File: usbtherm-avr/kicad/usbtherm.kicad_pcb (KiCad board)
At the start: 2 copper layers, 18 parts, among them IC1 ATMEGA328-P, P1 USB_A, Q1 TMP36, Y1 12 MHz

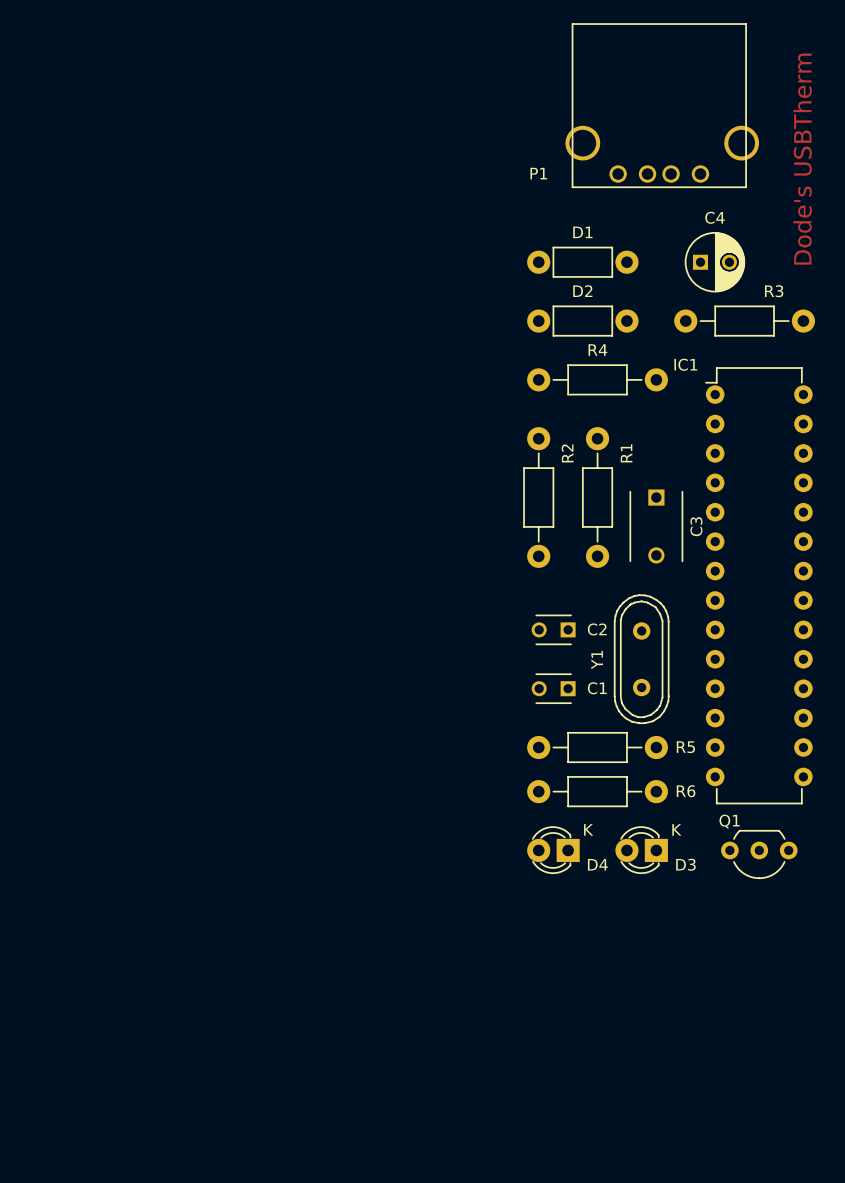
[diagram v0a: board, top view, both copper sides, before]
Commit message: replaced USB connector with plug, created footprint for it, added board edges, autorouted with FreeRouting, fixed offset of 3D model of resistors
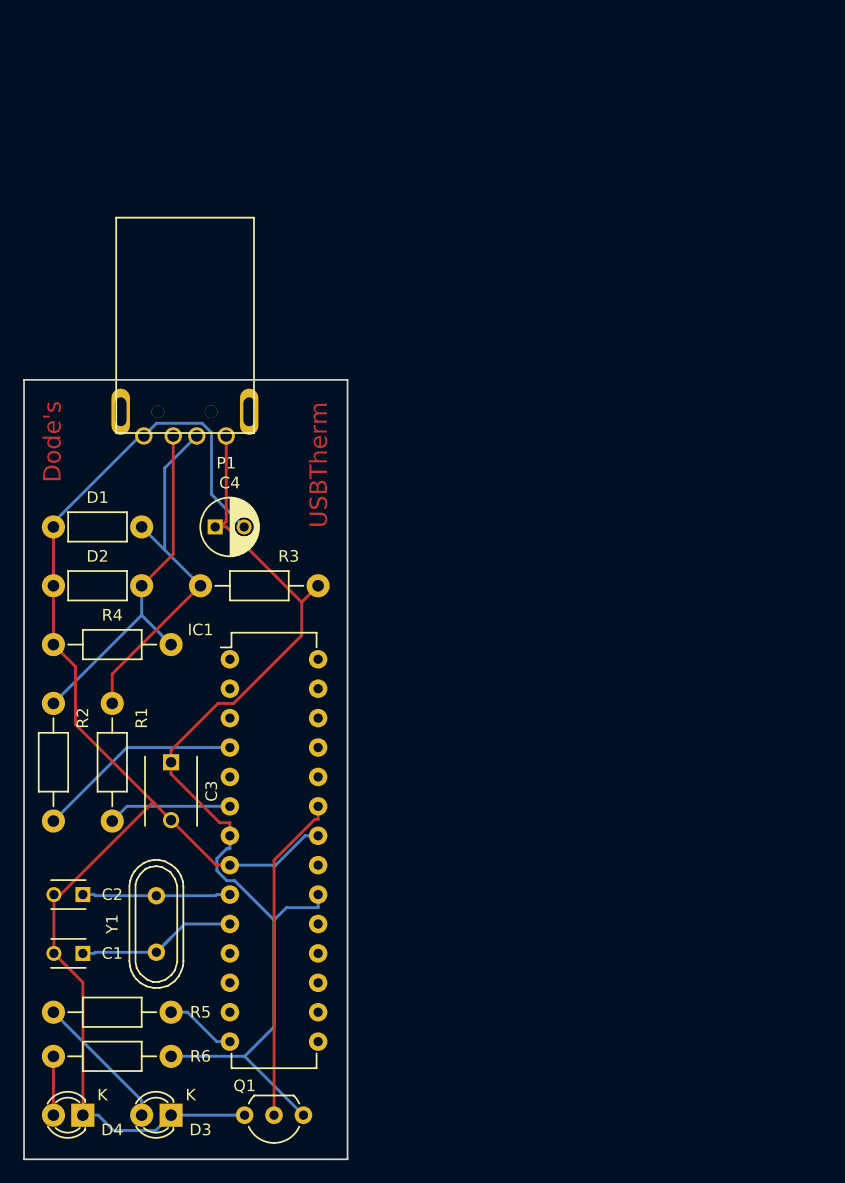
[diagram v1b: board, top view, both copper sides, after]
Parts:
- P1: value USB_A -> USB_A_PLUG; footprint Connect:USB_A -> Connect:USB_A_PLUG
- moved D1 47.7 mm to (139.7, 86.4)
- moved D2 47.7 mm to (139.7, 91.4)
- moved Q1 47.7 mm to (153.7, 137.2)
- moved C3 47.7 mm to (142.2, 106.7)
- moved R5 47.7 mm to (132.1, 128.3)
- moved R6 47.7 mm to (142.2, 132.1)
- moved C1 47.7 mm to (134.6, 123.2)
- moved C2 47.7 mm to (134.6, 118.1)
- moved C4 47.7 mm to (146.1, 86.4)
- moved D3 47.7 mm to (142.2, 137.2)
- moved D4 47.7 mm to (134.6, 137.2)
- moved IC1 47.7 mm to (147.3, 97.8)
- moved R1 47.7 mm to (137.2, 101.6)
- moved R2 47.7 mm to (132.1, 101.6)
- moved R3 47.7 mm to (154.9, 91.4)
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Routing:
- net GND: track 0.00 -> 119.5 mm
- net Net-(C3-Pad1): track 0.00 -> 90.6 mm
- net Net-(D1-Pad1): track 0.00 -> 31.5 mm
- net Net-(D2-Pad1): track 0.00 -> 31.0 mm
- net Net-(IC1-Pad23): track 0.00 -> 28.4 mm
- net Net-(IC1-Pad4): track 0.00 -> 17.9 mm
- net Net-(C1-Pad1): track 0.00 -> 15.5 mm
- net Net-(C2-Pad1): track 0.00 -> 12.8 mm
- net Net-(D3-Pad2): track 0.00 -> 12.0 mm
- net Net-(IC1-Pad6): track 0.00 -> 10.7 mm
- net Net-(IC1-Pad14): track 0.00 -> 6.13 mm
- net Net-(D4-Pad2): track 0.00 -> 5.08 mm
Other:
- board outline added: 27.9 x 67.3 mm
- board text added: "Dode's"
- board text added: "USBTherm"
- board text removed: "Dode's USBTherm"

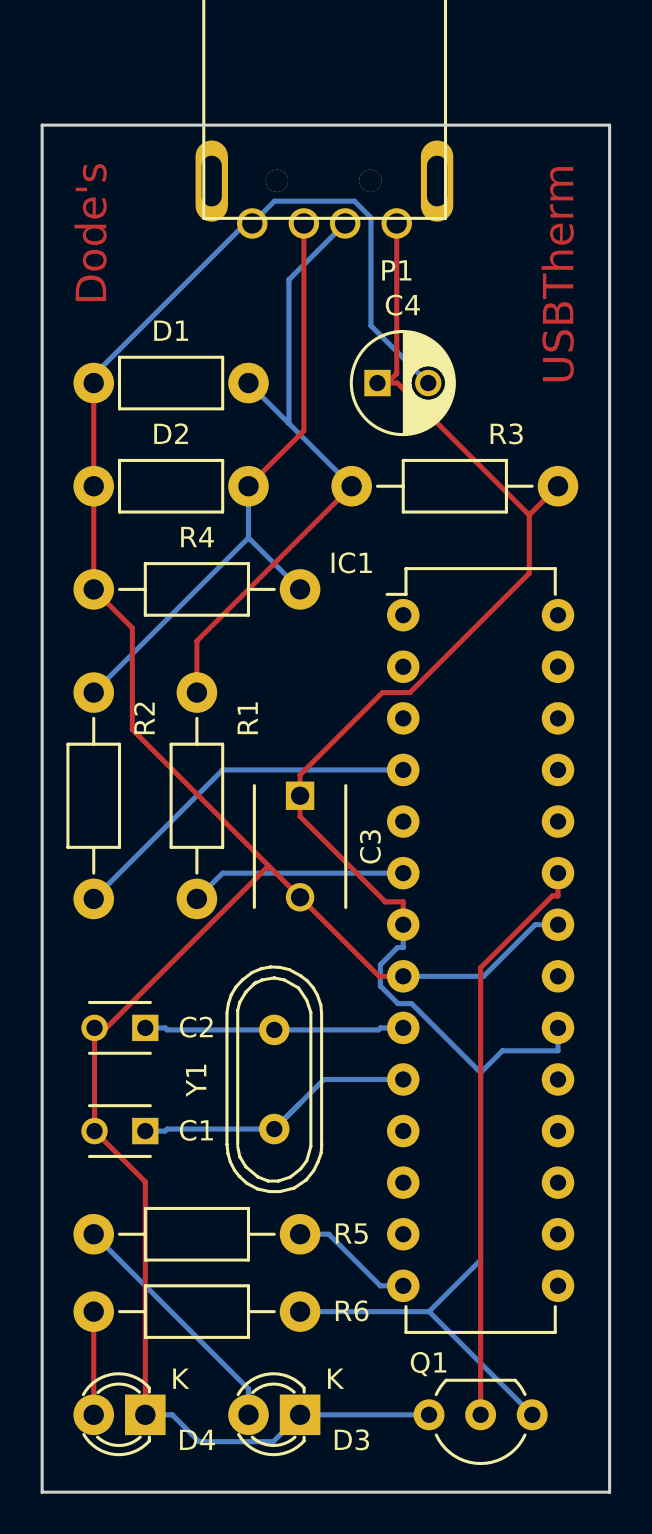
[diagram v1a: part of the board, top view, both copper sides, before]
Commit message: fixed 2 DRC warnings, added ground plane
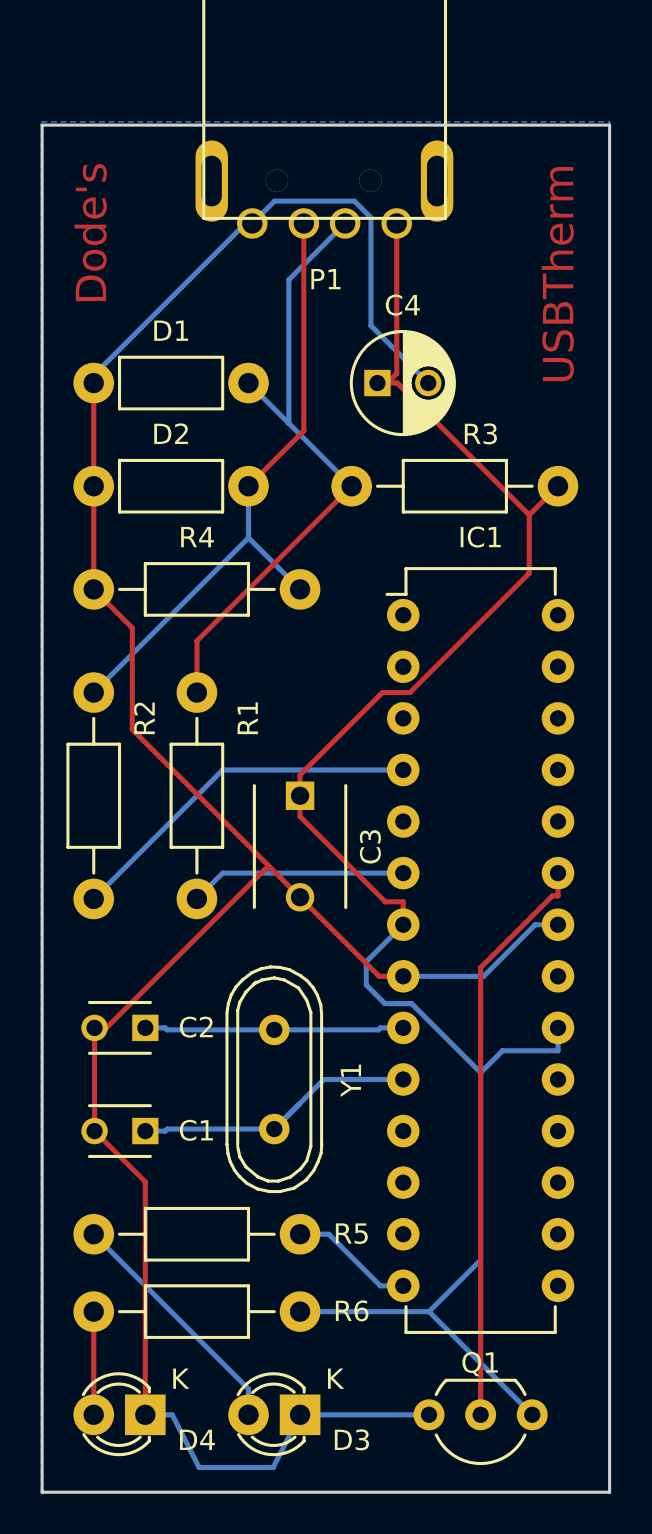
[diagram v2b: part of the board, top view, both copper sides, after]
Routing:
- net GND: track 119.5 -> 121.6 mm
- net Net-(C3-Pad1): track 90.6 -> 92.0 mm
- added copper zone on B.Cu, net GND
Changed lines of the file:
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@@
     (descr "28-lead dip package, row spacing 7.62 mm (300 mils)")
     (tags "dil dip 2.54 300")
-    (fp_text reference IC1 (at -2.54 -2.54) (layer F.SilkS)
+    (fp_text reference IC1 (at 3.81 -3.81) (layer F.SilkS)
       (effects (font (size 1 1) (thickness 0.15)))
     )
@@
     (descr "TO-92 leads in-line, wide, drill 0.8mm (see NXP sot054_po.pdf)")
     (tags "to-92 sc-43 sc-43a sot54 PA33 transistor")
-    (fp_text reference Q1 (at 5.08 2.54 360) (layer F.SilkS)
-      (effects (font (size 1 1) (thickness 0.15)))
-    )
-    (fp_text value TMP36 (at 1.27 2.54 180) (layer F.Fab)
+    (fp_text reference Q1 (at 2.54 2.54 360) (layer F.SilkS)
+      (effects (font (size 1 1) (thickness 0.15)))
+    )
+    (fp_text value TMP36 (at 2.54 -2.54 180) (layer F.Fab)
       (effects (font (size 1 1) (thickness 0.15)))
     )
@@
     (descr "Resistor, Axial,  RM 10mm, 1/3W")
     (tags "Resistor Axial RM 10mm 1/3W")
-    (fp_text reference R3 (at 2.54 2.54 180) (layer F.SilkS)
+    (fp_text reference R3 (at 3.81 2.54 180) (layer F.SilkS)
       (effects (font (size 1 1) (thickness 0.15)))
     )
@@
     (descr "Crystal, Quarz, HC49/U, vertical, stehend,")
     (tags "Crystal, Quarz, HC49/U, vertical, stehend,")
-    (fp_text reference Y1 (at 0 -3.81 90) (layer F.SilkS)
-      (effects (font (size 1 1) (thickness 0.15)))
-    )
-    (fp_text value "12 MHz" (at 0 3.81 90) (layer F.Fab)
+    (fp_text reference Y1 (at 0 3.81 90) (layer F.SilkS)
+      (effects (font (size 1 1) (thickness 0.15)))
+    )
+    (fp_text value "12 MHz" (at 0 0 90) (layer F.Fab)
       (effects (font (size 1 1) (thickness 0.15)))
     )
@@
     (descr "USB A Plug")
     (tags "USB USB_A PLUG")
-    (fp_text reference P1 (at 0 -2.35 180) (layer F.SilkS)
+    (fp_text reference P1 (at 3.49 -2.78 180) (layer F.SilkS)
       (effects (font (size 1 1) (thickness 0.15)))
     )
@@
   )
   (segment (start 143.411 120.65) (end 142.1905 121.8705) (width 0.25) (layer B.Cu) (net 1))
-  (segment (start 147.32 120.65) (end 143.411 120.65) (width 0.25) (layer B.Cu) (net 1))
+  (segment (start 147.32 120.65) (end 143.411 120.65) (width 0.25) (layer B.Cu) (net 1) (status 10))
   (segment (start 135.595 123.19) (end 134.62 123.19) (width 0.25) (layer B.Cu) (net 1))
   (segment (start 135.694 123.091) (end 135.595 123.19) (width 0.25) (layer B.Cu) (net 1))
@@
   (segment (start 148.59 137.16) (end 142.24 137.16) (width 0.25) (layer B.Cu) (net 2))
   (segment (start 135.945 137.16) (end 134.62 137.16) (width 0.25) (layer B.Cu) (net 2))
-  (segment (start 137.271 138.485) (end 135.945 137.16) (width 0.25) (layer B.Cu) (net 2))
-  (segment (start 140.915 138.485) (end 137.271 138.485) (width 0.25) (layer B.Cu) (net 2))
-  (segment (start 142.24 137.16) (end 140.915 138.485) (width 0.25) (layer B.Cu) (net 2))
-  (segment (start 151.275 115.57) (end 147.32 115.57) (width 0.25) (layer B.Cu) (net 2))
+  (segment (start 137.271 139.755) (end 135.945 137.16) (width 0.25) (layer B.Cu) (net 2))
+  (segment (start 140.915 139.755) (end 137.271 139.755) (width 0.25) (layer B.Cu) (net 2))
+  (segment (start 142.24 137.16) (end 140.915 139.755) (width 0.25) (layer B.Cu) (net 2))
+  (segment (start 151.275 115.57) (end 147.32 115.57) (width 0.25) (layer B.Cu) (net 2) (status 20))
   (segment (start 153.815 113.03) (end 151.275 115.57) (width 0.25) (layer B.Cu) (net 2))
-  (segment (start 154.94 113.03) (end 153.815 113.03) (width 0.25) (layer B.Cu) (net 2))
+  (segment (start 154.94 113.03) (end 153.815 113.03) (width 0.25) (layer B.Cu) (net 2) (status 10))
   (segment (start 146.13 115.57) (end 142.24 111.68) (width 0.25) (layer F.Cu) (net 2))
-  (segment (start 147.32 115.57) (end 146.13 115.57) (width 0.25) (layer F.Cu) (net 2))
+  (segment (start 147.32 115.57) (end 146.13 115.57) (width 0.25) (layer F.Cu) (net 2) (status 10))
   (segment (start 132.08 91.44) (end 132.08 86.36) (width 0.25) (layer F.Cu) (net 2))
   (segment (start 132.08 96.52) (end 132.08 91.44) (width 0.25) (layer F.Cu) (net 2))
@@
   (segment (start 135.595 118.11) (end 135.694 118.209) (width 0.25) (layer B.Cu) (net 3))
   (segment (start 134.62 118.11) (end 135.595 118.11) (width 0.25) (layer B.Cu) (net 3))
-  (segment (start 146.195 118.11) (end 147.32 118.11) (width 0.25) (layer B.Cu) (net 3))
+  (segment (start 146.195 118.11) (end 147.32 118.11) (width 0.25) (layer B.Cu) (net 3) (status 20))
   (segment (start 146.096 118.209) (end 146.195 118.11) (width 0.25) (layer B.Cu) (net 3))
   (segment (start 140.9699 118.209) (end 146.096 118.209) (width 0.25) (layer B.Cu) (net 3))
   (segment (start 140.9699 118.209) (end 140.97 118.2091) (width 0.25) (layer B.Cu) (net 3))
+  (segment (start 147.908 117.092) (end 147.73 116.914) (width 0.25) (layer B.Cu) (net 4))
+  (segment (start 147.73 116.914) (end 146.414 116.914) (width 0.25) (layer B.Cu) (net 4))
+  (segment (start 145.5 114.85) (end 147.32 113.03) (width 0.25) (layer B.Cu) (net 4))
+  (segment (start 145.5 116) (end 145.5 114.85) (width 0.25) (layer B.Cu) (net 4))
+  (segment (start 146.414 116.914) (end 145.5 116) (width 0.25) (layer B.Cu) (net 4))
   (segment (start 154.94 91.44) (end 153.523 92.8573) (width 0.25) (layer F.Cu) (net 4))
   (segment (start 153.523 95.7246) (end 153.523 92.8573) (width 0.25) (layer F.Cu) (net 4))
@@
   (segment (start 142.24 105.655) (end 146.295 101.6) (width 0.25) (layer F.Cu) (net 4))
   (segment (start 142.24 106.68) (end 142.24 105.655) (width 0.25) (layer F.Cu) (net 4))
-  (segment (start 147.73 116.914) (end 151.13 120.314) (width 0.25) (layer B.Cu) (net 4))
+  (segment (start 147.908 117.092) (end 151.13 120.314) (width 0.25) (layer B.Cu) (net 4))
   (segment (start 147.06 116.914) (end 147.73 116.914) (width 0.25) (layer B.Cu) (net 4))
-  (segment (start 146.195 116.049) (end 147.06 116.914) (width 0.25) (layer B.Cu) (net 4))
-  (segment (start 146.195 114.999) (end 146.195 116.049) (width 0.25) (layer B.Cu) (net 4))
-  (segment (start 147.039 114.155) (end 146.195 114.999) (width 0.25) (layer B.Cu) (net 4))
-  (segment (start 147.32 114.155) (end 147.039 114.155) (width 0.25) (layer B.Cu) (net 4))
-  (segment (start 147.32 113.03) (end 147.32 114.155) (width 0.25) (layer B.Cu) (net 4))
-  (segment (start 154.94 119.235) (end 154.94 118.11) (width 0.25) (layer B.Cu) (net 4))
+  (segment (start 154.94 119.235) (end 154.94 118.11) (width 0.25) (layer B.Cu) (net 4) (status 20))
   (segment (start 152.209 119.235) (end 154.94 119.235) (width 0.25) (layer B.Cu) (net 4))
   (segment (start 151.13 120.314) (end 152.209 119.235) (width 0.25) (layer B.Cu) (net 4))
   (segment (start 151.13 129.54) (end 148.59 132.08) (width 0.25) (layer B.Cu) (net 4))
   (segment (start 151.13 120.314) (end 151.13 129.54) (width 0.25) (layer B.Cu) (net 4))
-  (segment (start 147.32 111.905) (end 147.32 113.03) (width 0.25) (layer F.Cu) (net 4))
+  (segment (start 147.32 111.905) (end 147.32 113.03) (width 0.25) (layer F.Cu) (net 4) (status 20))
   (segment (start 146.439 111.905) (end 147.32 111.905) (width 0.25) (layer F.Cu) (net 4))
   (segment (start 142.24 107.705) (end 146.439 111.905) (width 0.25) (layer F.Cu) (net 4))
@@
   (segment (start 132.08 128.27) (end 139.7 135.89) (width 0.25) (layer B.Cu) (net 7))
   (segment (start 132.08 132.08) (end 132.08 137.16) (width 0.25) (layer F.Cu) (net 8))
-  (segment (start 138.43 105.41) (end 147.32 105.41) (width 0.25) (layer B.Cu) (net 12))
+  (segment (start 138.43 105.41) (end 147.32 105.41) (width 0.25) (layer B.Cu) (net 12) (status 20))
   (segment (start 132.08 111.76) (end 138.43 105.41) (width 0.25) (layer B.Cu) (net 12))
-  (segment (start 138.43 110.49) (end 147.32 110.49) (width 0.25) (layer B.Cu) (net 14))
+  (segment (start 138.43 110.49) (end 147.32 110.49) (width 0.25) (layer B.Cu) (net 14) (status 20))
   (segment (start 137.16 111.76) (end 138.43 110.49) (width 0.25) (layer B.Cu) (net 14))
   (segment (start 143.655 128.27) (end 142.24 128.27) (width 0.25) (layer B.Cu) (net 18))
   (segment (start 146.195 130.81) (end 143.655 128.27) (width 0.25) (layer B.Cu) (net 18))
-  (segment (start 147.32 130.81) (end 146.195 130.81) (width 0.25) (layer B.Cu) (net 18))
+  (segment (start 147.32 130.81) (end 146.195 130.81) (width 0.25) (layer B.Cu) (net 18) (status 10))
   (segment (start 151.13 115.144) (end 151.13 137.16) (width 0.25) (layer F.Cu) (net 25))
   (segment (start 154.659 111.615) (end 151.13 115.144) (width 0.25) (layer F.Cu) (net 25))
   (segment (start 154.94 111.615) (end 154.659 111.615) (width 0.25) (layer F.Cu) (net 25))
-  (segment (start 154.94 110.49) (end 154.94 111.615) (width 0.25) (layer F.Cu) (net 25))
+  (segment (start 154.94 110.49) (end 154.94 111.615) (width 0.25) (layer F.Cu) (net 25) (status 10))
+  (zone (net 2) (net_name GND) (layer B.Cu) (hatch edge 0.508)
+    (connect_pads (clearance 0.508))
+    (min_thickness 0.254)
+    (fill yes (arc_segments 16) (thermal_gap 0.508) (thermal_bridge_width 0.508))
+    (polygon
+      (pts
+        (xy 129.5 73.5) (xy 157.5 73.5) (xy 157.5 141) (xy 129.5 141)
+      )
+    )
+  )
 )

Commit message: modified the silk screen of the USB plug to not extend the board edges and changed the oval drills for the shield pins to circular so it looks okay at OSHPark
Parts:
- P1: footprint Connect:USB_A_PLUG -> Connect:USB_A_PLUG_CIRCULAR
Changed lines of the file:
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@@
       (net 3 "Net-(C2-Pad1)"))
   )
-  (module Connect:USB_A_PLUG (layer F.Cu)
+  (module Connect:USB_A_PLUG_CIRCULAR (layer F.Cu)
     (at 147 78.5 180)
     (descr "USB A Plug")
     (tags "USB USB_A PLUG")
-    (fp_text reference P1 (at 3.49 -2.78 180) (layer F.SilkS)
+    (fp_text reference P1 (at 0 -2.35 180) (layer F.SilkS)
       (effects (font (size 1 1) (thickness 0.15)))
     )
@@
     )
     (fp_line (start -2.4 0.25) (end 9.5 0.25) (layer F.SilkS) (width 0.15))
-    (fp_line (start 9.5 0.25) (end 9.5 18.85) (layer F.SilkS) (width 0.15))
-    (fp_line (start 9.5 18.85) (end -2.4 18.85) (layer F.SilkS) (width 0.15))
-    (fp_line (start -2.4 18.85) (end -2.4 0.25) (layer F.SilkS) (width 0.15))
+    (fp_line (start 9.5 0.25) (end 9.5 4.8) (layer F.SilkS) (width 0.15))
+    (fp_line (start 9.5 4.8) (end -2.4 4.8) (layer F.SilkS) (width 0.15))
+    (fp_line (start -2.4 4.8) (end -2.4 0.25) (layer F.SilkS) (width 0.15))
     (fp_line (start -2 0.25) (end -1.95 0.25) (layer F.SilkS) (width 0.15))
     (fp_line (start -3.9 4.8) (end -3.9 -1.1) (layer F.CrtYd) (width 0.05))
@@
     (pad 1 thru_hole circle (at 0.00086 -0.00212 90) (size 1.50114 1.50114) (drill 1.00076) (layers *.Cu *.Mask F.SilkS)
       (net 4 "Net-(C3-Pad1)"))
-    (pad 6 thru_hole oval (at 9.11086 2.08488 90) (size 4 1.6) (drill oval 2.5 1) (layers *.Cu *.Mask F.SilkS))
-    (pad 5 thru_hole oval (at -1.98514 2.08488 90) (size 4 1.6) (drill oval 2.5 1) (layers *.Cu *.Mask F.SilkS)
+    (pad 6 thru_hole circle (at 9.11086 2.08488 90) (size 3.5 3.5) (drill 2.5) (layers *.Cu *.Mask F.SilkS))
+    (pad 5 thru_hole circle (at -1.98514 2.08488 90) (size 3.5 3.5) (drill 2.5) (layers *.Cu *.Mask F.SilkS)
       (net 31 "Net-(P1-Pad5)"))
     (pad 6 thru_hole circle (at 1.3 2.1 90) (size 1.1 1.1) (drill 1.1) (layers *.Cu *.Mask F.SilkS))
   )
-  (gr_text Dode's (at 132 79 90) (layer F.Cu)
+  (gr_text USBTherm (at 155 81 90) (layer F.SilkS)
+    (effects (font (size 1.5 1.5) (thickness 0.3)))
+  )
+  (gr_text Dode's (at 132 79 90) (layer F.SilkS)
     (effects (font (size 1.5 1.5) (thickness 0.3)))
   )
@@
   (gr_line (start 129.54 140.97) (end 157.48 140.97) (angle 90) (layer Edge.Cuts) (width 0.15))
   (gr_line (start 129.54 73.66) (end 129.54 140.97) (angle 90) (layer Edge.Cuts) (width 0.15))
-  (gr_text USBTherm (at 155 81 90) (layer F.Cu)
-    (effects (font (size 1.5 1.5) (thickness 0.3)))
-  )
   (segment (start 143.411 120.65) (end 142.1905 121.8705) (width 0.25) (layer B.Cu) (net 1))
   (segment (start 147.32 120.65) (end 143.411 120.65) (width 0.25) (layer B.Cu) (net 1) (status 10))
